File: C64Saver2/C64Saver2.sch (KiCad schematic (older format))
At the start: 21 parts, among them J1 Conn_01x04, J2 Conn_01x12, J3 Conn_01x12, J6 Conn_01x04, Q1 2N7002, Q2 Q_PMOS_GDS

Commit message: saver 2.0beta - addon 1.0beta
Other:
- note added: "2.0beta"
- note added: "BETA VERSION\nDo not order boards of this version !\n"
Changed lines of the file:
@@
 	0    -1   -1   0
 $EndComp
+Text Notes 10700 7650 0    60   ~ 0
+2.0beta
+Text Notes 5150 5850 0    197  ~ 0
+BETA VERSION\nDo not order boards of this version !\n
 $EndSCHEMATC

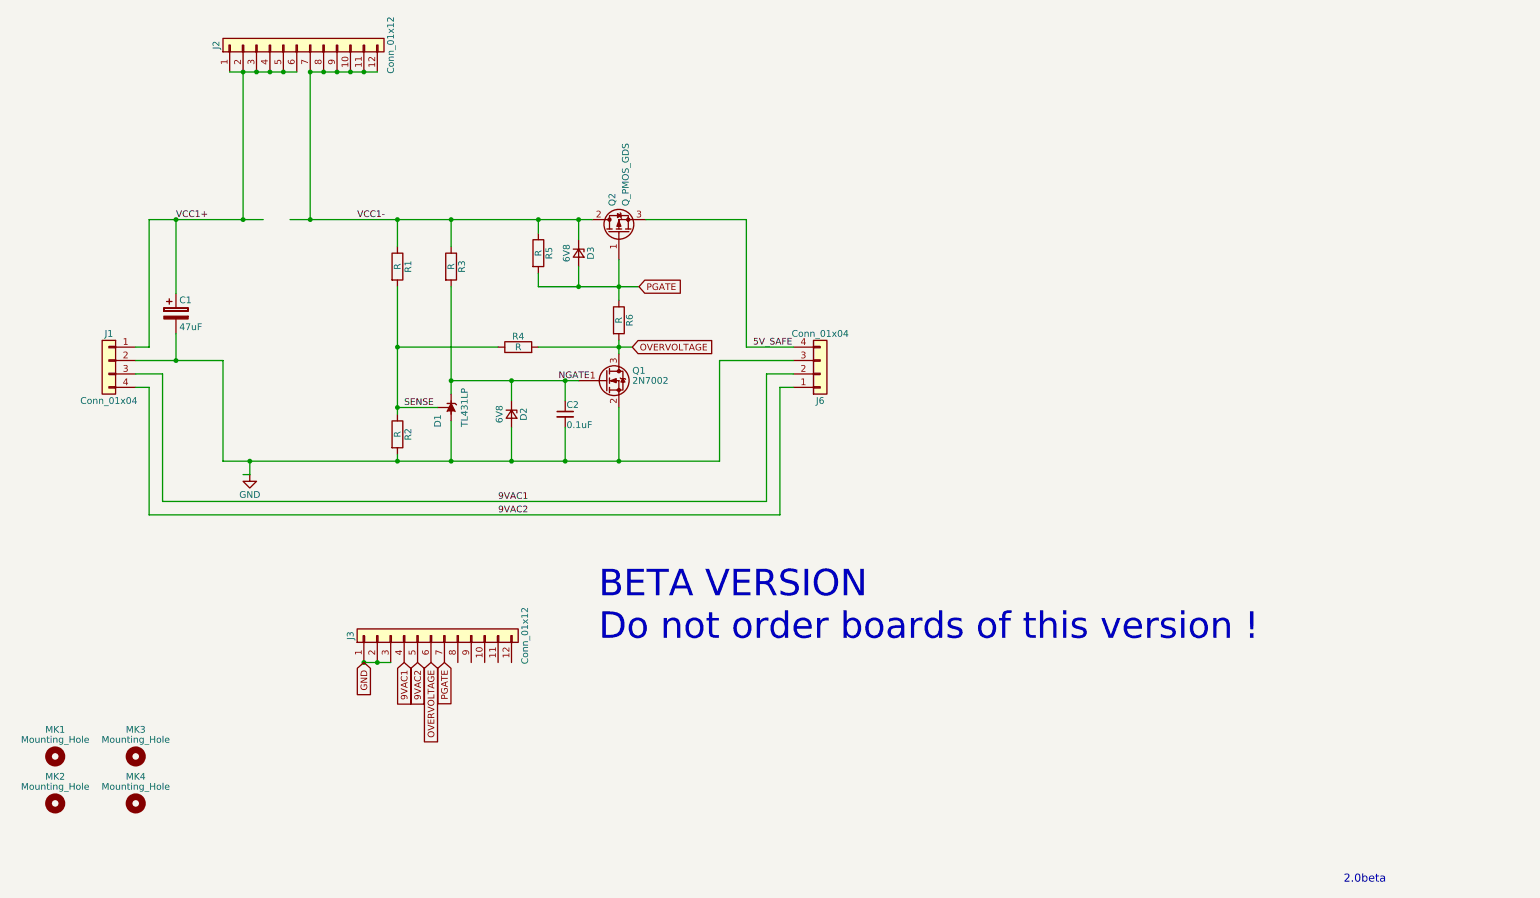
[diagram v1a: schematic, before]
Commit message: added gnd, 5x 9vac pins, moved c1 closer to input circuit
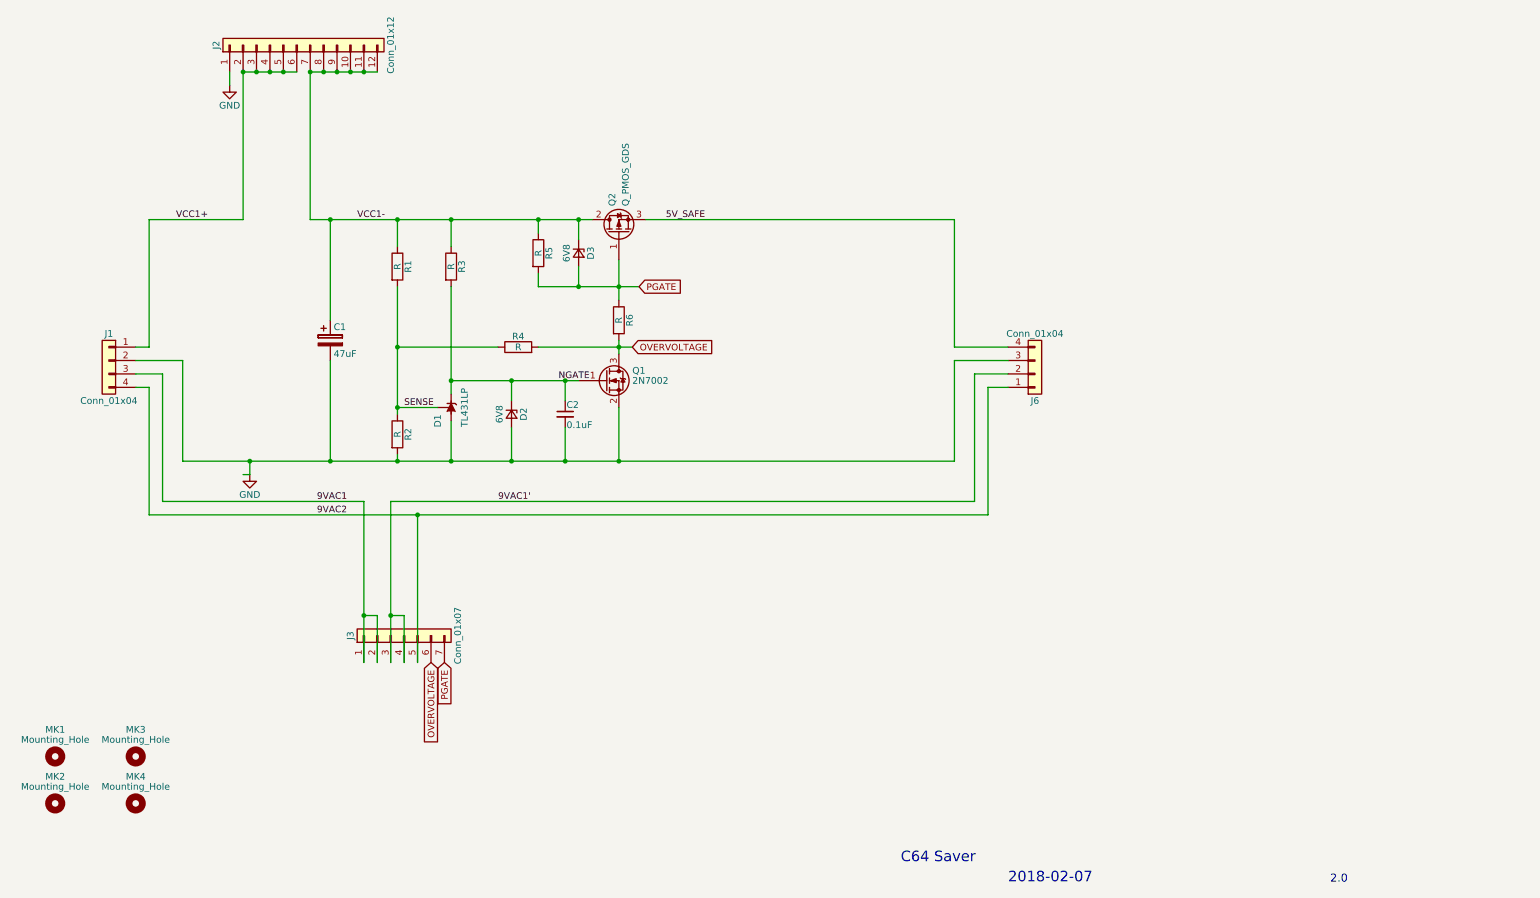
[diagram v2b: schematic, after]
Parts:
- removed J3: Conn_01x12, Pin_Headers:Pin_Header_Straight_1x12_Pitch2.54mm, symbol Conn_01x12
- added J3: Conn_01x07, Pin_Headers:Pin_Header_Straight_1x07_Pitch2.54mm, symbol Conn_01x07
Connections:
- net labels added: 9VAC1'
- wire segments 53 -> 61
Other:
- note added: "2.0"
- note added: "2018-02-07"
- note added: "C64 Saver"
- note removed: "2.0beta"
- note removed: "BETA VERSION\nDo not order boards of this version !\n"
- moved on the sheet: C1, J6
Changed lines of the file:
@@
 L CP C1
 U 1 1 5AFB3C02
-P 2000 3400
-F 0 "C1" H 2025 3500 50  0000 L CNN
-F 1 "47uF" H 2025 3300 50  0000 L CNN
-F 2 "Capacitors_THT:CP_Radial_D6.3mm_P2.50mm" H 2038 3250 50  0001 C CNN
-F 3 "" H 2000 3400 50  0001 C CNN
-	1    2000 3400
+P 3150 3600
+F 0 "C1" H 3175 3700 50  0000 L CNN
+F 1 "47uF" H 3175 3500 50  0000 L CNN
+F 2 "Capacitors_THT:CP_Radial_D6.3mm_P2.50mm" H 3188 3450 50  0001 C CNN
+F 3 "" H 3150 3600 50  0001 C CNN
+	1    3150 3600
 	1    0    0    -1
 $EndComp
@@
 L Conn_01x04 J6
 U 1 1 5B1D42F2
-P 6800 3850
-F 0 "J6" H 6800 4050 50  0000 C CNN
-F 1 "Conn_01x04" H 6800 3550 50  0000 C CNN
-F 2 "Connectors_Terminal_Blocks:TerminalBlock_bornier-4_P5.08mm" H 6800 3850 50  0001 C CNN
-F 3 "" H 6800 3850 50  0001 C CNN
-	1    6800 3850
+P 8400 3850
+F 0 "J6" H 8400 4050 50  0000 C CNN
+F 1 "Conn_01x04" H 8400 3550 50  0000 C CNN
+F 2 "Connectors_Terminal_Blocks:TerminalBlock_bornier-4_P5.08mm" H 8400 3850 50  0001 C CNN
+F 3 "" H 8400 3850 50  0001 C CNN
+	1    8400 3850
 	1    0    0    1
 $EndComp
@@
 PGATE
 Text Label 4400 4800 0    49   ~ 0
-9VAC1
-Text Label 4400 4900 0    49   ~ 0
+9VAC1'
+Text Label 3050 4900 0    49   ~ 0
 9VAC2
-Text Label 6300 3650 0    49   ~ 0
+Text Label 5650 2700 0    49   ~ 0
 5V_SAFE
 Text Label 2000 2700 0    49   ~ 0
@@
 	1    0    0    -1
 $EndComp
-Text GLabel 3400 6000 3    49   Input ~ 0
-GND
-Text GLabel 3700 6000 3    49   Input ~ 0
-9VAC1
-Text GLabel 3800 6000 3    49   Input ~ 0
-9VAC2
 Text GLabel 4000 6000 3    49   Input ~ 0
 PGATE
@@
 	4050 4500 4050 4200
 Wire Wire Line
-	2350 4500 6050 4500
+	2050 4500 7800 4500
 Wire Wire Line
 	3650 4500 3650 4450
@@
 Connection ~ 3650 4500
 Wire Wire Line
-	2350 3750 2350 4500
-Wire Wire Line
-	1700 3750 2350 3750
-Wire Wire Line
-	6050 4500 6050 3750
-Wire Wire Line
-	6050 3750 6600 3750
+	2050 3750 2050 4500
+Wire Wire Line
+	1700 3750 2050 3750
 Connection ~ 5300 4500
 Wire Wire Line
-	6600 3950 6500 3950
-Wire Wire Line
-	6500 3950 6500 4900
-Wire Wire Line
-	6500 4900 1800 4900
+	1800 4900 8050 4900
 Wire Wire Line
 	1700 3950 1800 3950
@@
 	1800 3950 1800 4900
 Wire Wire Line
-	6600 3850 6400 3850
-Wire Wire Line
-	6400 3850 6400 4800
-Wire Wire Line
-	6400 4800 1900 4800
-Wire Wire Line
 	1900 4800 1900 3850
 Wire Wire Line
@@
 	1700 3650 1800 3650
 Wire Wire Line
-	2850 2700 5100 2700
-Wire Wire Line
-	1800 2700 2650 2700
+	3000 2700 5100 2700
+Wire Wire Line
+	1800 2700 2500 2700
 Wire Wire Line
 	2500 4600 2550 4600
@@
 	2550 4600 2550 4500
 Connection ~ 2550 4500
-Connection ~ 3000 2700
-Connection ~ 2500 2700
-Wire Wire Line
-	2000 3250 2000 2700
-Connection ~ 2000 2700
-Wire Wire Line
-	2000 3550 2000 3750
-Connection ~ 2000 3750
-Wire Wire Line
-	6250 2700 6250 3650
-Wire Wire Line
-	6250 3650 6600 3650
 $Comp
 L TL431LP D1
@@
 NGATE
 Wire Wire Line
-	5300 3300 5300 3000
-Wire Wire Line
-	6250 2700 5500 2700
+	5300 3000 5300 3300
+Wire Wire Line
+	5500 2700 7800 2700
 $Comp
 L Mounting_Hole MK1
@@
 	2500 2700 2500 1600
 Wire Wire Line
-	3000 2700 3000 1600
-Wire Wire Line
-	2900 1600 2400 1600
-Wire Wire Line
 	3000 1600 3500 1600
 Connection ~ 3400 1600
@@
 Connection ~ 2700 1600
 Connection ~ 2600 1600
-Connection ~ 2500 1600
-$Comp
-L Conn_01x12 J3
-U 1 1 5B204E80
-P 3900 5800
-F 0 "J3" H 3900 6400 50  0000 C CNN
-F 1 "Conn_01x12" H 3900 5100 50  0000 C CNN
-F 2 "Pin_Headers:Pin_Header_Straight_1x12_Pitch2.54mm" H 3900 5800 50  0001 C CNN
-F 3 "" H 3900 5800 50  0001 C CNN
-	1    3900 5800
-	0    -1   -1   0
-$EndComp
-Wire Wire Line
-	3400 6000 3600 6000
-Connection ~ 3400 6000
-Connection ~ 3500 6000
 Wire Wire Line
 	5000 2850 5000 2700
@@
 	0    -1   -1   0
 $EndComp
-Text Notes 10700 7650 0    60   ~ 0
-2.0beta
-Text Notes 5150 5850 0    197  ~ 0
-BETA VERSION\nDo not order boards of this version !\n
+Text Notes 10600 7650 0    60   ~ 0
+2.0
+Connection ~ 3800 4900
+$Comp
+L Conn_01x07 J3
+U 1 1 5B3A920F
+P 3700 5800
+F 0 "J3" H 3700 6200 50  0000 C CNN
+F 1 "Conn_01x07" H 3700 5400 50  0000 C CNN
+F 2 "Pin_Headers:Pin_Header_Straight_1x07_Pitch2.54mm" H 3700 5800 50  0001 C CNN
+F 3 "" H 3700 5800 50  0001 C CNN
+	1    3700 5800
+	0    -1   -1   0
+$EndComp
+Wire Wire Line
+	3800 6000 3800 4900
+Text Notes 7400 7500 0    79   ~ 0
+C64 Saver
+Text Notes 8200 7650 0    79   ~ 0
+2018-02-07
+Wire Wire Line
+	3150 3450 3150 2700
+Wire Wire Line
+	3150 3750 3150 4500
+Connection ~ 3150 4500
+Wire Wire Line
+	3600 4800 3600 6000
+Wire Wire Line
+	3600 4800 7950 4800
+Wire Wire Line
+	3700 6000 3700 5650
+Wire Wire Line
+	3700 5650 3600 5650
+Connection ~ 3600 5650
+Wire Wire Line
+	8200 3650 7800 3650
+Wire Wire Line
+	7800 3650 7800 2700
+Wire Wire Line
+	7950 4800 7950 3850
+Wire Wire Line
+	7950 3850 8200 3850
+Wire Wire Line
+	8050 4900 8050 3950
+Wire Wire Line
+	8050 3950 8200 3950
+Wire Wire Line
+	7800 4500 7800 3750
+Wire Wire Line
+	7800 3750 8200 3750
+Wire Wire Line
+	3400 4800 3400 6000
+Text Label 3050 4800 0    49   ~ 0
+9VAC1
+Wire Wire Line
+	1900 4800 3400 4800
+Wire Wire Line
+	3400 5650 3500 5650
+Wire Wire Line
+	3500 5650 3500 6000
+Connection ~ 3400 5650
+Wire Wire Line
+	2500 1600 2900 1600
+Connection ~ 2500 1600
+$Comp
+L GND #PWR02
+U 1 1 5B3B30A4
+P 2400 1700
+F 0 "#PWR02" H 2400 1450 50  0001 C CNN
+F 1 "GND" H 2400 1550 50  0000 C CNN
+F 2 "" H 2400 1700 50  0001 C CNN
+F 3 "" H 2400 1700 50  0001 C CNN
+	1    2400 1700
+	1    0    0    -1
+$EndComp
+Wire Wire Line
+	2400 1700 2400 1600
+Wire Wire Line
+	3000 1600 3000 2700
+Connection ~ 3150 2700
 $EndSCHEMATC
